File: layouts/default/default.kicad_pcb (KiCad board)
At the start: 2 copper layers, 45 x 32 mm, 27 parts, among them U3 WioSX1262, U4 ProMicro_nRF52840

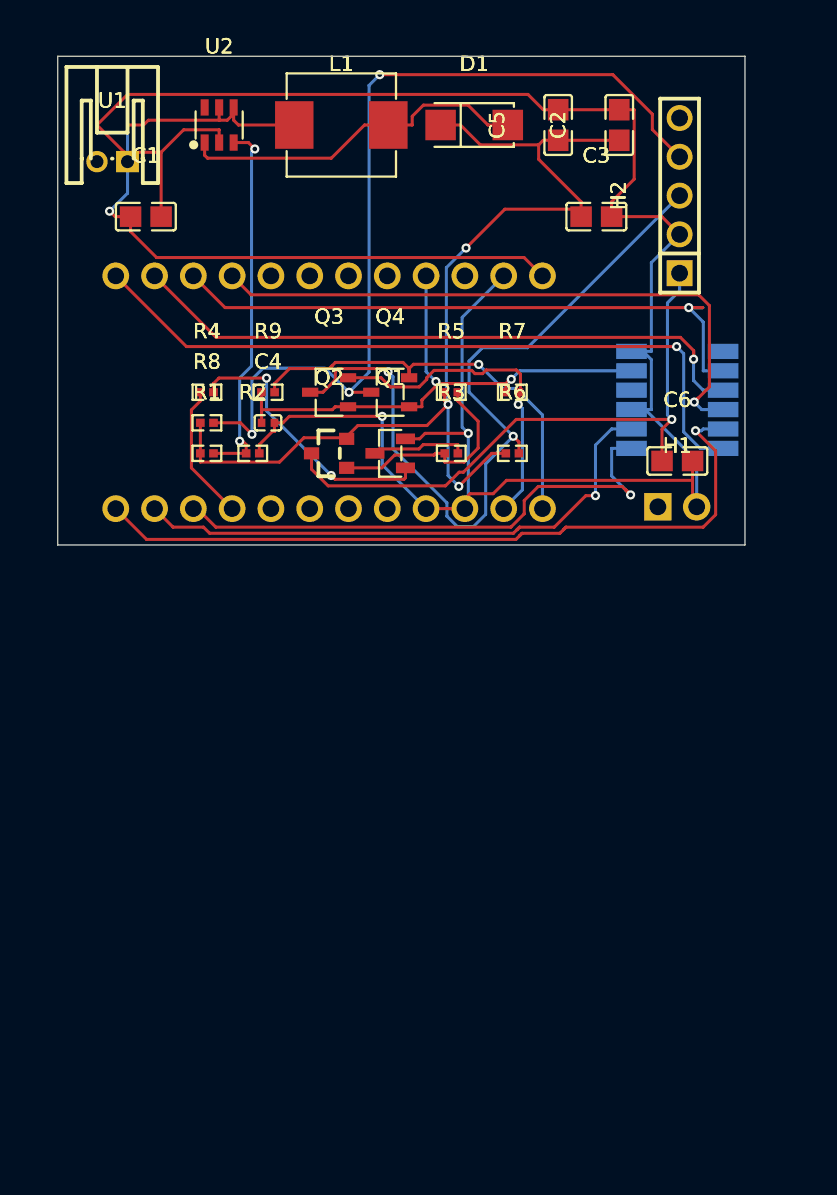
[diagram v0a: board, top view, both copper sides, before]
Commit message: Replace 5-pin RDM6300 header with 4-pin, fix WioSX1262 pad orientation
- Remove H1 (2-pin antenna header) and antenna signals from RDM6300
  module since the antenna is on the RDM6300 module itself
- Replace 5-pin header with 4-pin header (Ckmtw B-2100S04P-A110,
  LCSC C124378) for VCC, GND, TX, RX only
- Fix WioSX1262 pad dimensions from (1.6x0.6) to (0.6x1.6) to
  resolve DRC shorting violations at 1.27mm pitch
- Move silkscreen reference designators to Fab layer
- Remove silkscreen outlines from WioSX1262 footprint

Co-Authored-By: Claude Opus 4.5 <noreply@anthropic.com>
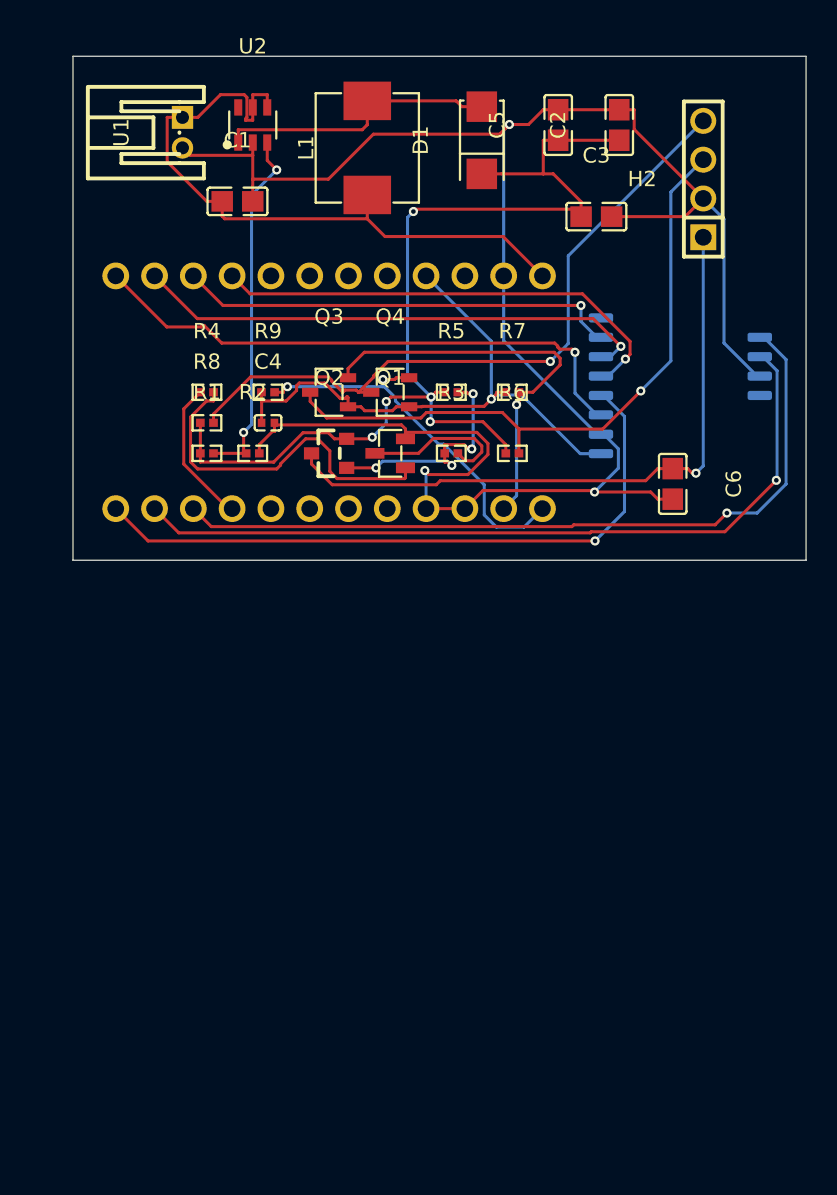
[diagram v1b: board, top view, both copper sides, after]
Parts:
- removed H1: , Ckmtw_B_2100S02P_A110:HDR-TH_2P-P2.54-V-M-1
- H2: footprint Ckmtw_B_2100S05P_A110:HDR-TH_5P-P2.54-V-M -> Ckmtw_B_2100S04P_A110:HDR-TH_4P-P2.54-V-M
- U3: value WioSX1262 -> (none)
- U4: value ProMicro_nRF52840 -> (none)
- moved U3 8.54 mm to (33.5, -24.2), turned to -90 degrees
- moved C1 6.08 mm to (10.0, -30.5)
- moved U1 4.98 mm to (6.40, -35.0), turned to 90 degrees
- moved L1 2.27 mm to (18.5, -34.0), turned to 90 degrees
- moved U2 2.20 mm to (11.0, -35.5)
- moved H2 1.89 mm to (40.5, -32.0)
- moved C6 1.53 mm to (38.5, -12.0), turned to -90 degrees
- moved D1 1.12 mm to (26.0, -34.5), turned to 90 degrees
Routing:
- net busy: track 36.9 -> 51.5 mm
- net MISO: track 42.8 -> 29.0 mm
- net rfid-uart-TX: track 59.3 -> 45.8 mm, vias 3 -> 1
- net dio1: track 37.8 -> 50.9 mm
- net GND: track 146.7 -> 133.7 mm, vias 2 -> 3
- net SCLK: track 42.3 -> 31.2 mm
- net cs: track 47.5 -> 37.2 mm
- net MOSI: track 43.8 -> 34.0 mm
- net rfid-uart-RX: track 51.9 -> 42.8 mm, vias 2 -> 1
- net footprint-reset-0: track 49.1 -> 43.3 mm
- net power_raw-VCC: track 49.8 -> 44.1 mm, vias 1 -> 0
- net mcu-uart-RX: track 21.8 -> 27.0 mm
- net footprint-G-0: track 18.0 -> 23.1 mm, vias 2 -> 0
- net A: track 23.1 -> 18.6 mm
- net D: track 6.24 -> 10.0 mm
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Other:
- board size 45 x 32 mm -> 48 x 33 mm

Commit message: Optimize power consumption and add mounting holes
- Replace BSS138 level shifter with voltage divider (100k/200k) for ~0µA idle
- Increase power switch resistors to 1MΩ for minimal idle current (~5µA)
- Add 4x M3 mounting holes at board corners
- Update placement.csv to avoid Pro Micro through-hole conflicts
- Add new resistor footprints for high-value components

Co-Authored-By: Claude Opus 4.5 <noreply@anthropic.com>
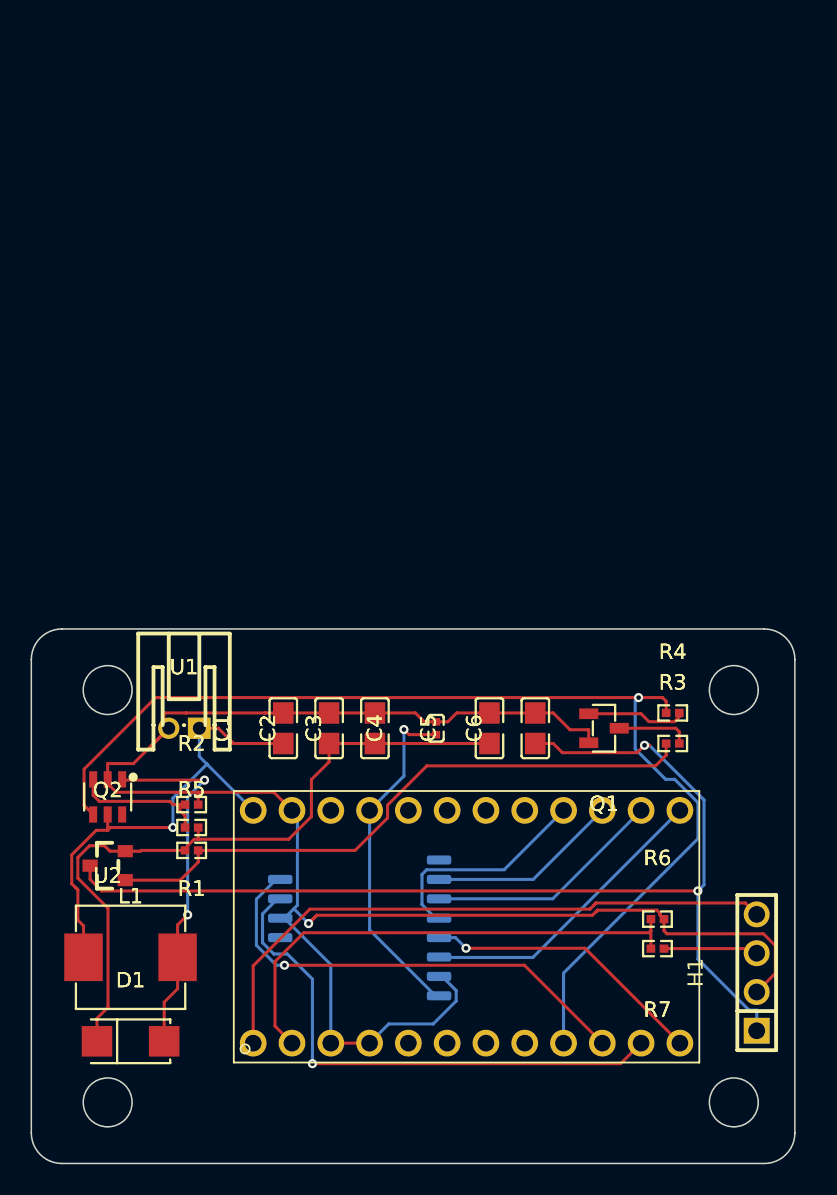
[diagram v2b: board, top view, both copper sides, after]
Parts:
- removed H2: , Ckmtw_B_2100S04P_A110:HDR-TH_4P-P2.54-V-M
- removed Q3, Q4: , onsemi_BSS138:SOT-23-3_L2.9-W1.6-P1.90-LS2.8-BR
- removed R8, R9: 10kΩ ±1% 62.5mW, UNI_ROYAL_0402WGF1002TCE:R0402
- added H1: , Ckmtw_B_2100S04P_A110:HDR-TH_4P-P2.54-V-M, F.Cu at (44.0, 20.0)
- R3: value 1kΩ ±1% 62.5mW -> 10kΩ ±1% 62.5mW; footprint UNI_ROYAL_0402WGF1001TCE:R0402 -> UNI_ROYAL_0402WGF1002TCE:R0402
- R4, R5: value 10kΩ ±1% 62.5mW -> 1MΩ ±1% 62.5mW; footprint UNI_ROYAL_0402WGF1002TCE:R0402 -> UNI_ROYAL_0402WGF1004TCE:R0402
- R6: value 10kΩ ±1% 62.5mW -> 200kΩ ±1% 62.5mW; footprint UNI_ROYAL_0402WGF1002TCE:R0402 -> FOJAN_FRC0402F2003TS:R0402
- R7: value 10kΩ ±1% 62.5mW -> 100kΩ ±1% 62.5mW; footprint UNI_ROYAL_0402WGF1002TCE:R0402 -> UNI_ROYAL_0402WGF1003TCE:R0402
- U4: moved to F.Cu
- moved D1 63.3 mm to (3.00, 24.5), turned to 0 degrees
- moved L1 55.2 mm to (3.00, 19.0), turned to 0 degrees
- moved U2 45.0 mm to (1.50, 8.50), turned to 180 degrees
- moved C2 43.8 mm to (16.0, 4.00)
- moved C5 39.8 mm to (26.5, 4.00)
- moved U1 39.0 mm to (6.50, 4.00), turned to 0 degrees
- moved R7 37.6 mm to (37.5, 18.4), turned to 180 degrees
- moved R4 37.0 mm to (38.5, 3.00)
- moved U3 36.9 mm to (23.5, 11.3)
- moved C3 36.5 mm to (19.0, 4.00), turned to 90 degrees
- moved U4 36.1 mm to (25.0, 17.0), turned to 0 degrees
- moved C1 34.6 mm to (13.0, 4.00), turned to 90 degrees
- moved R5 34.5 mm to (7.00, 12.0)
- moved R6 31.9 mm to (37.5, 16.5)
- moved Q2 30.6 mm to (1.50, 13.0)
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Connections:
- C2 pad 1: power_hv-VCC -> power_in-VCC
- C3 pad 1: power_hv-VCC -> power_in-VCC
- C4 pad 1: power_lv-VCC -> power_gnd-VCC
- C5 pad 1: power_hv-VCC -> power_in-VCC
- D1 pad 1: power_hv-VCC -> power_in-VCC
- Q2 pad 2: power_hv-VCC -> power_in-VCC
- R1 pad 1: power_hv-VCC -> power_in-VCC
- R5 pad 1: power_hv-VCC -> power_in-VCC
- R6 pad 1: power_hv-VCC -> mcu-uart-RX
- R6 pad 2: rfid-uart-RX -> GND
- R7 pad 1: power_lv-VCC -> rfid-uart-RX
- U2 pad 4: power_raw-VCC -> enable
- U3 pad 8: power_lv-VCC -> power_gnd-VCC
- U4 pad 1: mcu-uart-TX -> TX
- U4 pad 21: power_lv-VCC -> power_gnd-VCC
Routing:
- net power_hv-VCC: track 69.4 -> 0.00 mm, vias 5 -> 0
- net enable: track 9.53 -> 72.6 mm, vias 0 -> 1
- net power_in-VCC: track 0.00 -> 46.5 mm
- net rfid-uart-TX: track 45.8 -> 0.00 mm, vias 1 -> 0
- net TX: track 0.00 -> 40.3 mm
- net power_lv-VCC: track 39.1 -> 0.00 mm, vias 1 -> 0
- net rfid-uart-RX: track 42.8 -> 6.19 mm, vias 1 -> 0
- net power_out-VCC: track 42.6 -> 72.4 mm, vias 1 -> 2
- net mcu-uart-TX: track 25.6 -> 0.00 mm, vias 2 -> 0
- net footprint-G-1: track 15.5 -> 40.5 mm, vias 4 -> 0
- net footprint-reset-0: track 43.3 -> 18.6 mm
- net power_gnd-VCC: track 0.00 -> 22.6 mm, vias 0 -> 1
- net dio1: track 50.9 -> 30.4 mm
- net MOSI: track 34.0 -> 15.6 mm, vias 1 -> 0
- net cs: track 37.2 -> 19.8 mm, vias 1 -> 0
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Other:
- board size 48 x 33 mm -> 50 x 35 mm

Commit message: Update PCB layout
Co-Authored-By: Claude Opus 4.5 <noreply@anthropic.com>
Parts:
- U3: moved to F.Cu
- U4: moved to B.Cu
- turned U4 to 180 degrees
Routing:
- net power_raw-VCC: track 33.5 -> 81.3 mm
- net TX: track 40.3 -> 10.5 mm
- net mcu-uart-RX: track 33.2 -> 8.39 mm
- net GND: track 119.7 -> 103.3 mm, vias 1 -> 3
- net power_gnd-VCC: track 22.6 -> 36.5 mm, vias 1 -> 2
- net busy: track 35.3 -> 24.8 mm, vias 1 -> 0
- net enable: track 72.6 -> 64.4 mm, vias 1 -> 2
- net power_out-VCC: track 72.4 -> 78.2 mm
- net A: track 23.6 -> 29.3 mm
- net power_in-VCC: track 46.5 -> 41.7 mm
- net footprint-reset-0: track 18.6 -> 15.6 mm, vias 1 -> 0
- net MOSI: track 15.6 -> 12.6 mm
- net MISO: track 12.6 -> 9.56 mm
- net FB: track 8.97 -> 12.0 mm
- net SCLK: track 14.5 -> 12.2 mm
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
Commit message: Change battery connector to 2.54mm pitch header
- Replace JST-PH 2.0mm connector with 2.54mm pitch 2-pin header
- Add Header_2P_254 component (LCSC C124375)
- Update battery.ato to use new connector

Co-Authored-By: Claude Opus 4.5 <noreply@anthropic.com>
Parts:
- U1: footprint JST_Sales_America_S2B_PH_K_S_LF__SN:CONN-TH_S2B-PH-K-S-LF-SN -> Header_2P_254:HDR-TH_2P-P2.54-V
- moved U1 0.50 mm to (7.00, 4.00), turned to 90 degrees
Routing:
- net power_raw-VCC: track 81.3 -> 74.1 mm, vias 1 -> 0
- net power_gnd-VCC: track 36.5 -> 30.7 mm
- net A: track 29.3 -> 25.8 mm
- net FB: track 12.0 -> 8.69 mm
- net dio1: track 30.8 -> 33.3 mm
- net enable: track 64.4 -> 62.5 mm
- net cs: track 20.3 -> 22.1 mm
- net power_out-VCC: track 78.2 -> 79.2 mm
- net GND: track 103.3 -> 103.7 mm, vias 3 -> 1
